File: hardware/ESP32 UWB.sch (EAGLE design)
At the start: 54 parts, among them J2 HEADER-12P-2.54, J4 10118194-0001LF, Q3 S8050, Q4 S8050, U1 SILICON_LABS_CP2102N-A01-GQFN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, U2 V_REG_MIC2920, U5 DWM1000, U6 ESP32-C3-MINI-1-N4

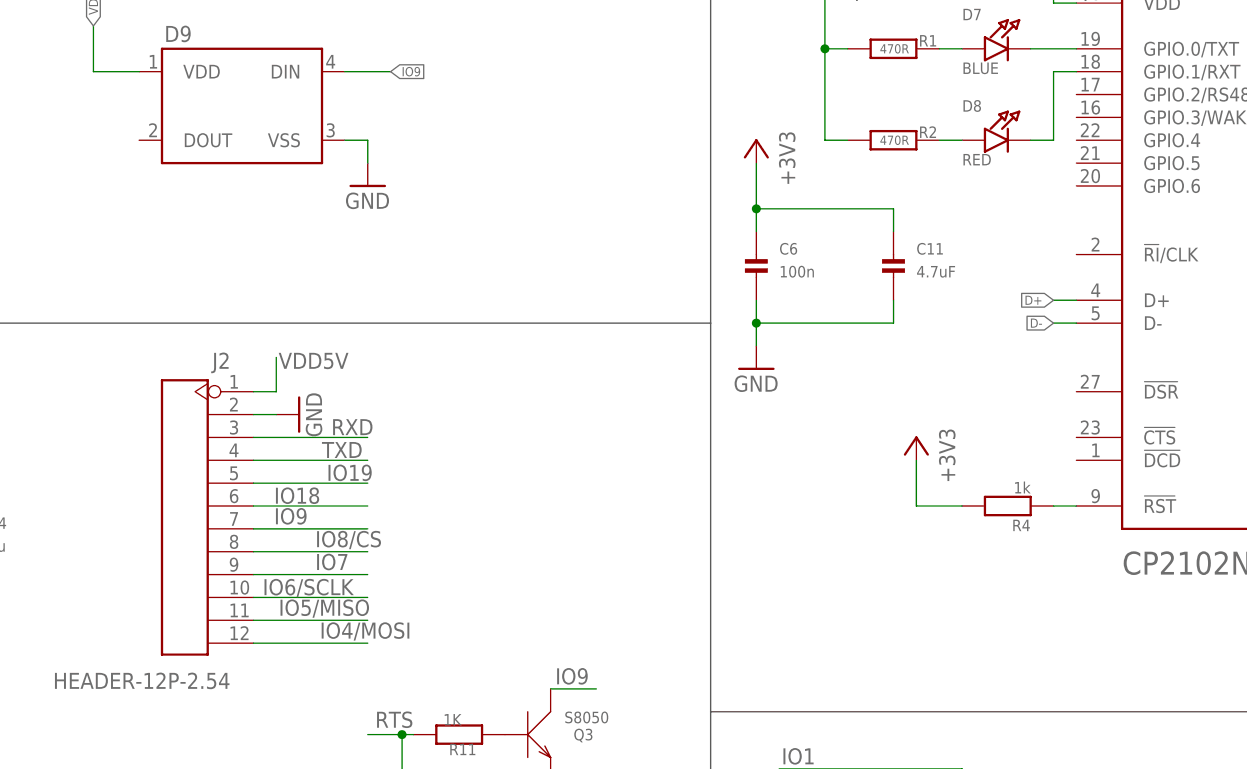
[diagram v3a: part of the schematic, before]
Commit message: fixed floating input pins
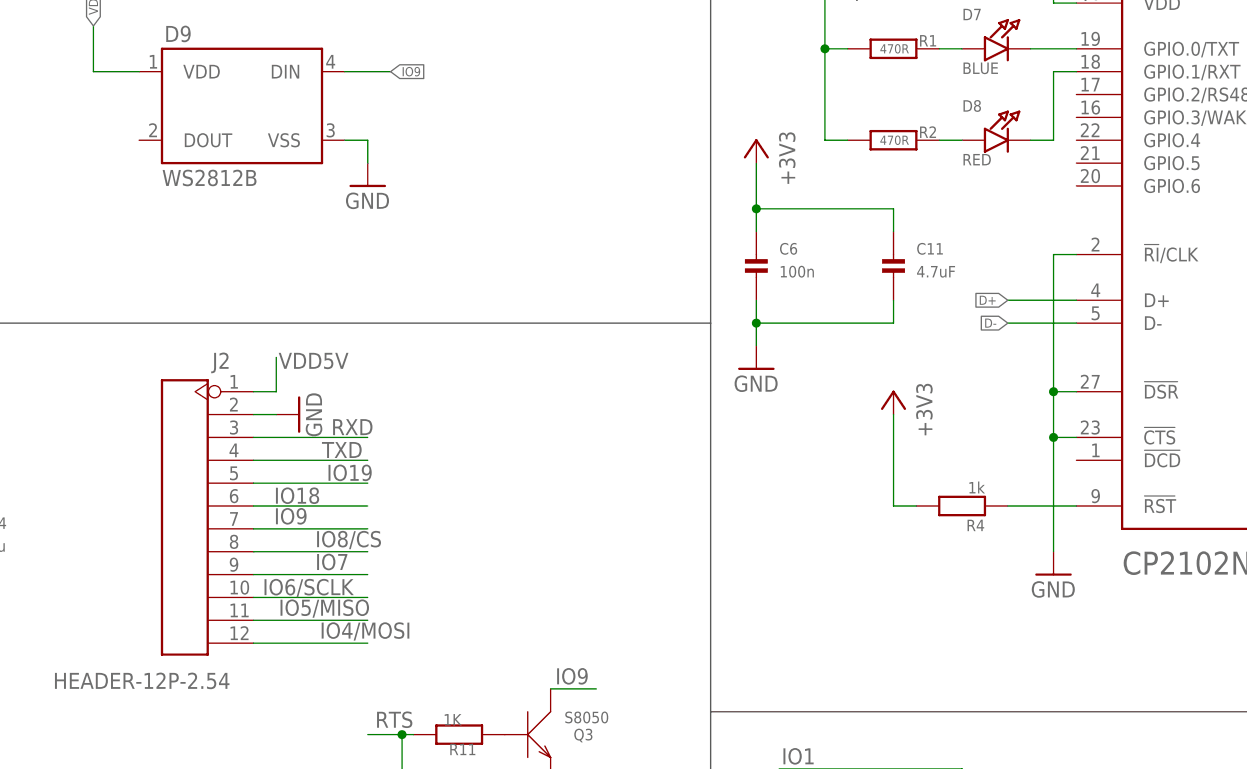
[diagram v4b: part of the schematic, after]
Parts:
- D9: value (none) -> WS2812B
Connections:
- net GND: now also U1.!CTS!, U1.!DSR!, U1.!RI!/CLK
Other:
- moved on the sheet: R4
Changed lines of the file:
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@@
 <part name="C5" library="isystems" deviceset="CAP_CERAMIC" device="0603" value="10u"/>
 <part name="C7" library="isystems" deviceset="CAP_CERAMIC" device="0603" value="100n"/>
-<part name="D9" library="SparkFun-LED" deviceset="WS2812B" device=""/>
+<part name="D9" library="SparkFun-LED" deviceset="WS2812B" device="" value="WS2812B"/>
 <part name="GND4" library="supply1" deviceset="GND" device=""/>
+<part name="GND5" library="SparkFun-Aesthetics" deviceset="GND" device=""/>
 </parts>
 <sheets>
@@
 <instance part="GND6" gate="1" x="144.78" y="15.24"/>
 <instance part="GND12" gate="1" x="170.18" y="137.16"/>
-<instance part="R4" gate="G$1" x="353.06" y="106.68" rot="R180"/>
-<instance part="+3V12" gate="G$1" x="342.9" y="114.3" rot="MR0"/>
+<instance part="R4" gate="G$1" x="347.98" y="106.68" rot="R180"/>
+<instance part="+3V12" gate="G$1" x="340.36" y="119.38" rot="MR0"/>
 <instance part="C14" gate="G$1" x="236.22" y="101.6"/>
 <instance part="C15" gate="G$1" x="226.06" y="101.6"/>
@@
 <instance part="D9" gate="G$1" x="261.62" y="149.86"/>
 <instance part="GND4" gate="1" x="281.94" y="142.24"/>
+<instance part="GND5" gate="1" x="358.14" y="99.06"/>
 </instances>
 <busses>
@@
 <wire x1="281.94" y1="147.32" x2="279.4" y2="147.32" width="0.1524" layer="91"/>
 </segment>
+<segment>
+<pinref part="U1" gate="G$0" pin="!RI!/CLK"/>
+<wire x1="360.68" y1="134.62" x2="358.14" y2="134.62" width="0.1524" layer="91"/>
+<pinref part="GND5" gate="1" pin="GND"/>
+<wire x1="358.14" y1="134.62" x2="358.14" y2="119.38" width="0.1524" layer="91"/>
+<pinref part="U1" gate="G$0" pin="!CTS!"/>
+<wire x1="358.14" y1="119.38" x2="358.14" y2="114.3" width="0.1524" layer="91"/>
+<wire x1="358.14" y1="114.3" x2="358.14" y2="101.6" width="0.1524" layer="91"/>
+<wire x1="360.68" y1="114.3" x2="358.14" y2="114.3" width="0.1524" layer="91"/>
+<junction x="358.14" y="114.3"/>
+<pinref part="U1" gate="G$0" pin="!DSR!"/>
+<wire x1="360.68" y1="119.38" x2="358.14" y2="119.38" width="0.1524" layer="91"/>
+<junction x="358.14" y="119.38"/>
+</segment>
 </net>
 <net name="+3V3" class="0">
@@
 <pinref part="R4" gate="G$1" pin="2"/>
 <pinref part="+3V12" gate="G$1" pin="+3V3"/>
-<wire x1="347.98" y1="106.68" x2="342.9" y2="106.68" width="0.1524" layer="91"/>
-<wire x1="342.9" y1="106.68" x2="342.9" y2="111.76" width="0.1524" layer="91"/>
+<wire x1="342.9" y1="106.68" x2="340.36" y2="106.68" width="0.1524" layer="91"/>
+<wire x1="340.36" y1="106.68" x2="340.36" y2="116.84" width="0.1524" layer="91"/>
 </segment>
 </net>
@@
 <net name="D+" class="0">
 <segment>
-<wire x1="358.14" y1="129.54" x2="360.68" y2="129.54" width="0.1524" layer="91"/>
+<wire x1="353.06" y1="129.54" x2="360.68" y2="129.54" width="0.1524" layer="91"/>
 <pinref part="U1" gate="G$0" pin="D+"/>
-<label x="358.14" y="129.54" size="1.016" layer="95" rot="R180" xref="yes"/>
+<label x="353.06" y="129.54" size="1.016" layer="95" rot="R180" xref="yes"/>
 </segment>
 <segment>
@@
 <net name="D-" class="0">
 <segment>
-<wire x1="358.14" y1="127" x2="360.68" y2="127" width="0.1524" layer="91"/>
+<wire x1="353.06" y1="127" x2="360.68" y2="127" width="0.1524" layer="91"/>
 <pinref part="U1" gate="G$0" pin="D-"/>
-<label x="358.14" y="127" size="1.016" layer="95" rot="R180" xref="yes"/>
+<label x="353.06" y="127" size="1.016" layer="95" rot="R180" xref="yes"/>
 </segment>
 <segment>
@@
 <pinref part="R4" gate="G$1" pin="1"/>
 <pinref part="U1" gate="G$0" pin="!RST!"/>
-<wire x1="358.14" y1="106.68" x2="360.68" y2="106.68" width="0.1524" layer="91"/>
-</segment>
-</net>
+<wire x1="353.06" y1="106.68" x2="360.68" y2="106.68" width="0.1524" layer="91"/>
+</segment>
+</net>

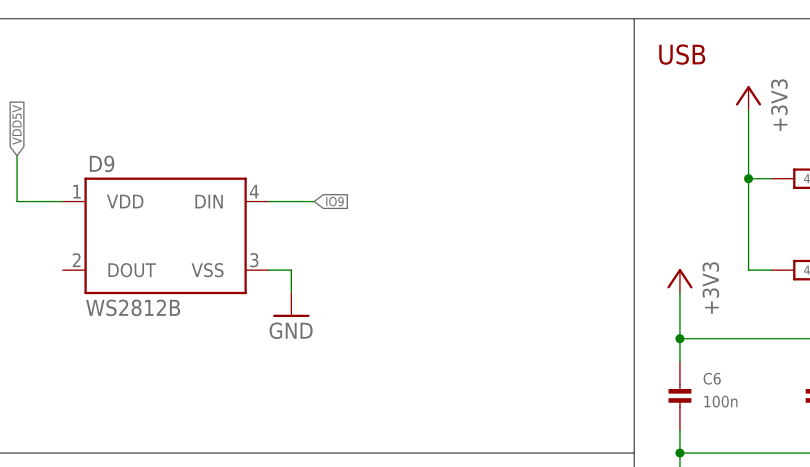
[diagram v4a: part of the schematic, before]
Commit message: added solder jumper for optionally disabling the ws2812 led
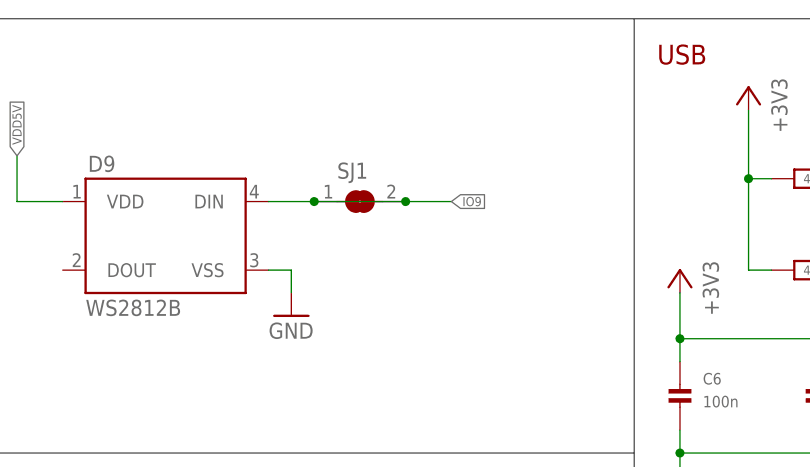
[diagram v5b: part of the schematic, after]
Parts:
- added SJ1: (no value), jumper:SJ
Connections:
- net IO9: now also SJ1.1, SJ1.2
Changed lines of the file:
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@@
 <part name="GND4" library="supply1" deviceset="GND" device=""/>
 <part name="GND5" library="SparkFun-Aesthetics" deviceset="GND" device=""/>
+<part name="SJ1" library="jumper" deviceset="SJ" device=""/>
 </parts>
 <sheets>
@@
 <instance part="GND4" gate="1" x="281.94" y="142.24"/>
 <instance part="GND5" gate="1" x="358.14" y="99.06"/>
+<instance part="SJ1" gate="1" x="289.56" y="154.94"/>
 </instances>
 <busses>
@@
 <pinref part="D9" gate="G$1" pin="DIN"/>
 <wire x1="279.4" y1="154.94" x2="284.48" y2="154.94" width="0.1524" layer="91"/>
-<label x="284.48" y="154.94" size="1.016" layer="95" xref="yes"/>
-</segment>
-</net>
+<label x="299.72" y="154.94" size="1.016" layer="95" xref="yes"/>
+<pinref part="SJ1" gate="1" pin="2"/>
+<wire x1="284.48" y1="154.94" x2="294.64" y2="154.94" width="0.1524" layer="91"/>
+<wire x1="294.64" y1="154.94" x2="299.72" y2="154.94" width="0.1524" layer="91"/>
+<junction x="294.64" y="154.94"/>
+<pinref part="SJ1" gate="1" pin="1"/>
+<junction x="284.48" y="154.94"/>
+</segment>
+</net>

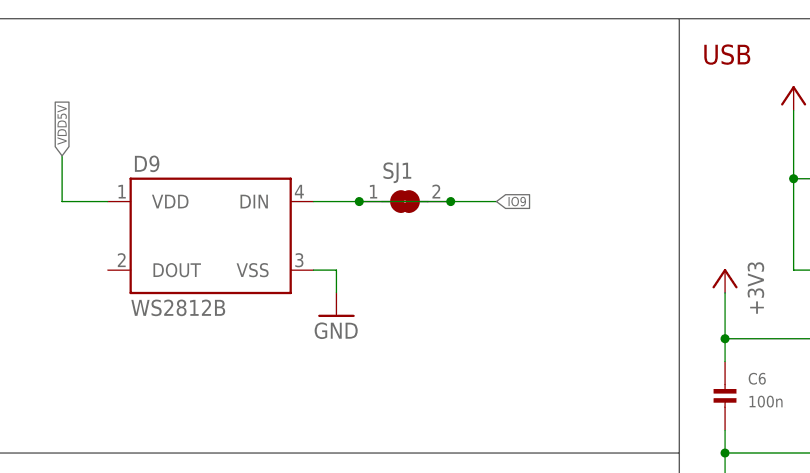
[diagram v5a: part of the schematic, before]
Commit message: Updated SJ Package to my own (smaller) version
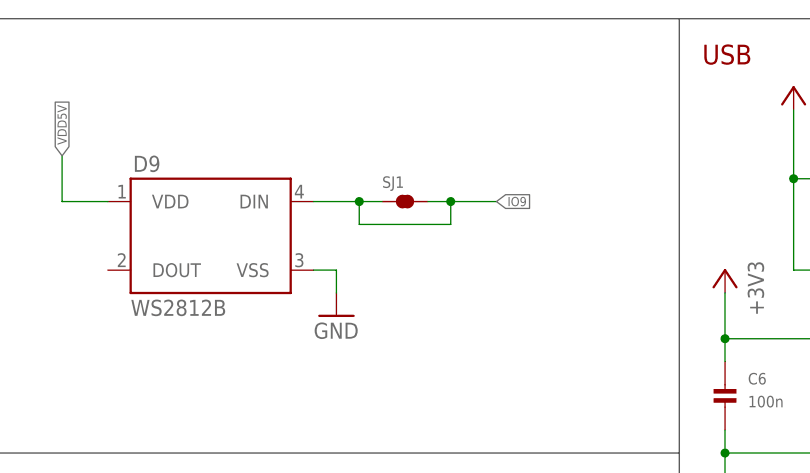
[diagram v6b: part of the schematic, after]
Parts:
- SJ1: device jumper:SJ -> isystems:SJS
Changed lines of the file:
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@@
 <grid distance="0.1" unitdist="inch" unit="inch" style="lines" multiple="1" display="no" altdistance="0.01" altunitdist="inch" altunit="inch"/>
 <layers>
-<layer number="1" name="Top" color="4" fill="1" visible="yes" active="no"/>
-<layer number="2" name="Route2" color="1" fill="3" visible="yes" active="no"/>
-<layer number="3" name="Route3" color="4" fill="3" visible="yes" active="no"/>
-<layer number="4" name="Route4" color="1" fill="4" visible="yes" active="no"/>
-<layer number="5" name="Route5" color="4" fill="4" visible="yes" active="no"/>
-<layer number="6" name="Route6" color="1" fill="8" visible="yes" active="no"/>
-<layer number="7" name="Route7" color="4" fill="8" visible="yes" active="no"/>
-<layer number="8" name="Route8" color="1" fill="2" visible="yes" active="no"/>
-<layer number="9" name="Route9" color="4" fill="2" visible="yes" active="no"/>
-<layer number="10" name="Route10" color="1" fill="7" visible="yes" active="no"/>
-<layer number="11" name="Route11" color="4" fill="7" visible="yes" active="no"/>
-<layer number="12" name="Route12" color="1" fill="5" visible="yes" active="no"/>
-<layer number="13" name="Route13" color="4" fill="5" visible="yes" active="no"/>
-<layer number="14" name="Route14" color="1" fill="6" visible="yes" active="no"/>
-<layer number="15" name="Route15" color="4" fill="6" visible="yes" active="no"/>
-<layer number="16" name="Bottom" color="1" fill="1" visible="yes" active="no"/>
-<layer number="17" name="Pads" color="2" fill="1" visible="yes" active="no"/>
-<layer number="18" name="Vias" color="2" fill="1" visible="yes" active="no"/>
-<layer number="19" name="Unrouted" color="6" fill="1" visible="yes" active="no"/>
-<layer number="20" name="Dimension" color="15" fill="1" visible="yes" active="no"/>
-<layer number="21" name="tPlace" color="7" fill="1" visible="yes" active="no"/>
-<layer number="22" name="bPlace" color="7" fill="1" visible="yes" active="no"/>
-<layer number="23" name="tOrigins" color="15" fill="1" visible="yes" active="no"/>
-<layer number="24" name="bOrigins" color="15" fill="1" visible="yes" active="no"/>
-<layer number="25" name="tNames" color="7" fill="1" visible="yes" active="no"/>
-<layer number="26" name="bNames" color="7" fill="1" visible="yes" active="no"/>
-<layer number="27" name="tValues" color="7" fill="1" visible="yes" active="no"/>
-<layer number="28" name="bValues" color="7" fill="1" visible="yes" active="no"/>
+<layer number="1" name="Top" color="4" fill="1" visible="no" active="no"/>
+<layer number="2" name="Route2" color="1" fill="3" visible="no" active="no"/>
+<layer number="3" name="Route3" color="4" fill="3" visible="no" active="no"/>
+<layer number="4" name="Route4" color="1" fill="4" visible="no" active="no"/>
+<layer number="5" name="Route5" color="4" fill="4" visible="no" active="no"/>
+<layer number="6" name="Route6" color="1" fill="8" visible="no" active="no"/>
+<layer number="7" name="Route7" color="4" fill="8" visible="no" active="no"/>
+<layer number="8" name="Route8" color="1" fill="2" visible="no" active="no"/>
+<layer number="9" name="Route9" color="4" fill="2" visible="no" active="no"/>
+<layer number="10" name="Route10" color="1" fill="7" visible="no" active="no"/>
+<layer number="11" name="Route11" color="4" fill="7" visible="no" active="no"/>
+<layer number="12" name="Route12" color="1" fill="5" visible="no" active="no"/>
+<layer number="13" name="Route13" color="4" fill="5" visible="no" active="no"/>
+<layer number="14" name="Route14" color="1" fill="6" visible="no" active="no"/>
+<layer number="15" name="Route15" color="4" fill="6" visible="no" active="no"/>
+<layer number="16" name="Bottom" color="1" fill="1" visible="no" active="no"/>
+<layer number="17" name="Pads" color="2" fill="1" visible="no" active="no"/>
+<layer number="18" name="Vias" color="2" fill="1" visible="no" active="no"/>
+<layer number="19" name="Unrouted" color="6" fill="1" visible="no" active="no"/>
+<layer number="20" name="Dimension" color="15" fill="1" visible="no" active="no"/>
+<layer number="21" name="tPlace" color="7" fill="1" visible="no" active="no"/>
+<layer number="22" name="bPlace" color="7" fill="1" visible="no" active="no"/>
+<layer number="23" name="tOrigins" color="15" fill="1" visible="no" active="no"/>
+<layer number="24" name="bOrigins" color="15" fill="1" visible="no" active="no"/>
+<layer number="25" name="tNames" color="7" fill="1" visible="no" active="no"/>
+<layer number="26" name="bNames" color="7" fill="1" visible="no" active="no"/>
+<layer number="27" name="tValues" color="7" fill="1" visible="no" active="no"/>
+<layer number="28" name="bValues" color="7" fill="1" visible="no" active="no"/>
 <layer number="29" name="tStop" color="7" fill="3" visible="no" active="no"/>
 <layer number="30" name="bStop" color="7" fill="6" visible="no" active="no"/>
@@
 <layer number="35" name="tGlue" color="7" fill="4" visible="no" active="no"/>
 <layer number="36" name="bGlue" color="7" fill="5" visible="no" active="no"/>
-<layer number="37" name="tTest" color="7" fill="1" visible="yes" active="no"/>
-<layer number="38" name="bTest" color="7" fill="1" visible="yes" active="no"/>
+<layer number="37" name="tTest" color="7" fill="1" visible="no" active="no"/>
+<layer number="38" name="bTest" color="7" fill="1" visible="no" active="no"/>
 <layer number="39" name="tKeepout" color="4" fill="11" visible="no" active="no"/>
 <layer number="40" name="bKeepout" color="1" fill="11" visible="no" active="no"/>
@@
 <layer number="44" name="Drills" color="7" fill="1" visible="no" active="no"/>
 <layer number="45" name="Holes" color="7" fill="1" visible="no" active="no"/>
-<layer number="46" name="Milling" color="3" fill="1" visible="yes" active="no"/>
-<layer number="47" name="Measures" color="7" fill="1" visible="yes" active="no"/>
-<layer number="48" name="Document" color="7" fill="1" visible="yes" active="no"/>
-<layer number="49" name="Reference" color="7" fill="1" visible="yes" active="no"/>
-<layer number="50" name="dxf" color="7" fill="1" visible="yes" active="no"/>
-<layer number="51" name="tDocu" color="7" fill="1" visible="yes" active="no"/>
-<layer number="52" name="bDocu" color="7" fill="1" visible="yes" active="no"/>
-<layer number="53" name="tGND_GNDA" color="7" fill="9" visible="yes" active="no"/>
-<layer number="54" name="bGND_GNDA" color="1" fill="9" visible="yes" active="no"/>
-<layer number="56" name="wert" color="7" fill="1" visible="yes" active="no"/>
-<layer number="57" name="tCAD" color="7" fill="1" visible="yes" active="no"/>
-<layer number="59" name="tCarbon" color="7" fill="1" visible="yes" active="no"/>
-<layer number="60" name="bCarbon" color="7" fill="1" visible="yes" active="no"/>
+<layer number="46" name="Milling" color="3" fill="1" visible="no" active="no"/>
+<layer number="47" name="Measures" color="7" fill="1" visible="no" active="no"/>
+<layer number="48" name="Document" color="7" fill="1" visible="no" active="no"/>
+<layer number="49" name="Reference" color="7" fill="1" visible="no" active="no"/>
+<layer number="50" name="dxf" color="7" fill="1" visible="no" active="no"/>
+<layer number="51" name="tDocu" color="7" fill="1" visible="no" active="no"/>
+<layer number="52" name="bDocu" color="7" fill="1" visible="no" active="no"/>
+<layer number="53" name="tGND_GNDA" color="7" fill="9" visible="no" active="no"/>
+<layer number="54" name="bGND_GNDA" color="1" fill="9" visible="no" active="no"/>
+<layer number="56" name="wert" color="7" fill="1" visible="no" active="no"/>
+<layer number="57" name="tCAD" color="7" fill="1" visible="no" active="no"/>
+<layer number="59" name="tCarbon" color="7" fill="1" visible="no" active="no"/>
+<layer number="60" name="bCarbon" color="7" fill="1" visible="no" active="no"/>
 <layer number="88" name="SimResults" color="9" fill="1" visible="yes" active="yes"/>
 <layer number="89" name="SimProbes" color="9" fill="1" visible="yes" active="yes"/>
@@
 <part name="GND4" library="supply1" deviceset="GND" device=""/>
 <part name="GND5" library="SparkFun-Aesthetics" deviceset="GND" device=""/>
-<part name="SJ1" library="jumper" deviceset="SJ" device=""/>
+<part name="SJ1" library="isystems" deviceset="SJ" device="S"/>
 </parts>
 <sheets>
@@
 </segment>
 <segment>
-<pinref part="D9" gate="G$1" pin="DIN"/>
-<wire x1="279.4" y1="154.94" x2="284.48" y2="154.94" width="0.1524" layer="91"/>
 <label x="299.72" y="154.94" size="1.016" layer="95" xref="yes"/>
 <pinref part="SJ1" gate="1" pin="2"/>
-<wire x1="284.48" y1="154.94" x2="294.64" y2="154.94" width="0.1524" layer="91"/>
+<wire x1="292.1" y1="154.94" x2="294.64" y2="154.94" width="0.1524" layer="91"/>
+<pinref part="SJ1" gate="1" pin="1"/>
+<pinref part="D9" gate="G$1" pin="DIN"/>
 <wire x1="294.64" y1="154.94" x2="299.72" y2="154.94" width="0.1524" layer="91"/>
+<wire x1="279.4" y1="154.94" x2="284.48" y2="154.94" width="0.1524" layer="91"/>
+<wire x1="284.48" y1="154.94" x2="287.02" y2="154.94" width="0.1524" layer="91"/>
+<wire x1="284.48" y1="154.94" x2="284.48" y2="152.4" width="0.1524" layer="91"/>
+<junction x="284.48" y="154.94"/>
+<wire x1="284.48" y1="152.4" x2="294.64" y2="152.4" width="0.1524" layer="91"/>
+<wire x1="294.64" y1="152.4" x2="294.64" y2="154.94" width="0.1524" layer="91"/>
 <junction x="294.64" y="154.94"/>
-<pinref part="SJ1" gate="1" pin="1"/>
-<junction x="284.48" y="154.94"/>
-</segment>
-</net>
+</segment>
+</net>
